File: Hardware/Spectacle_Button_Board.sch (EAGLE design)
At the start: 53 parts, among them J17 AUDIO-JACK3, J19 FTDI_DEVICE, J20 AUDIO-JACK3, U1 CY8C4146LQI-S422, U2 3.3V/150mA

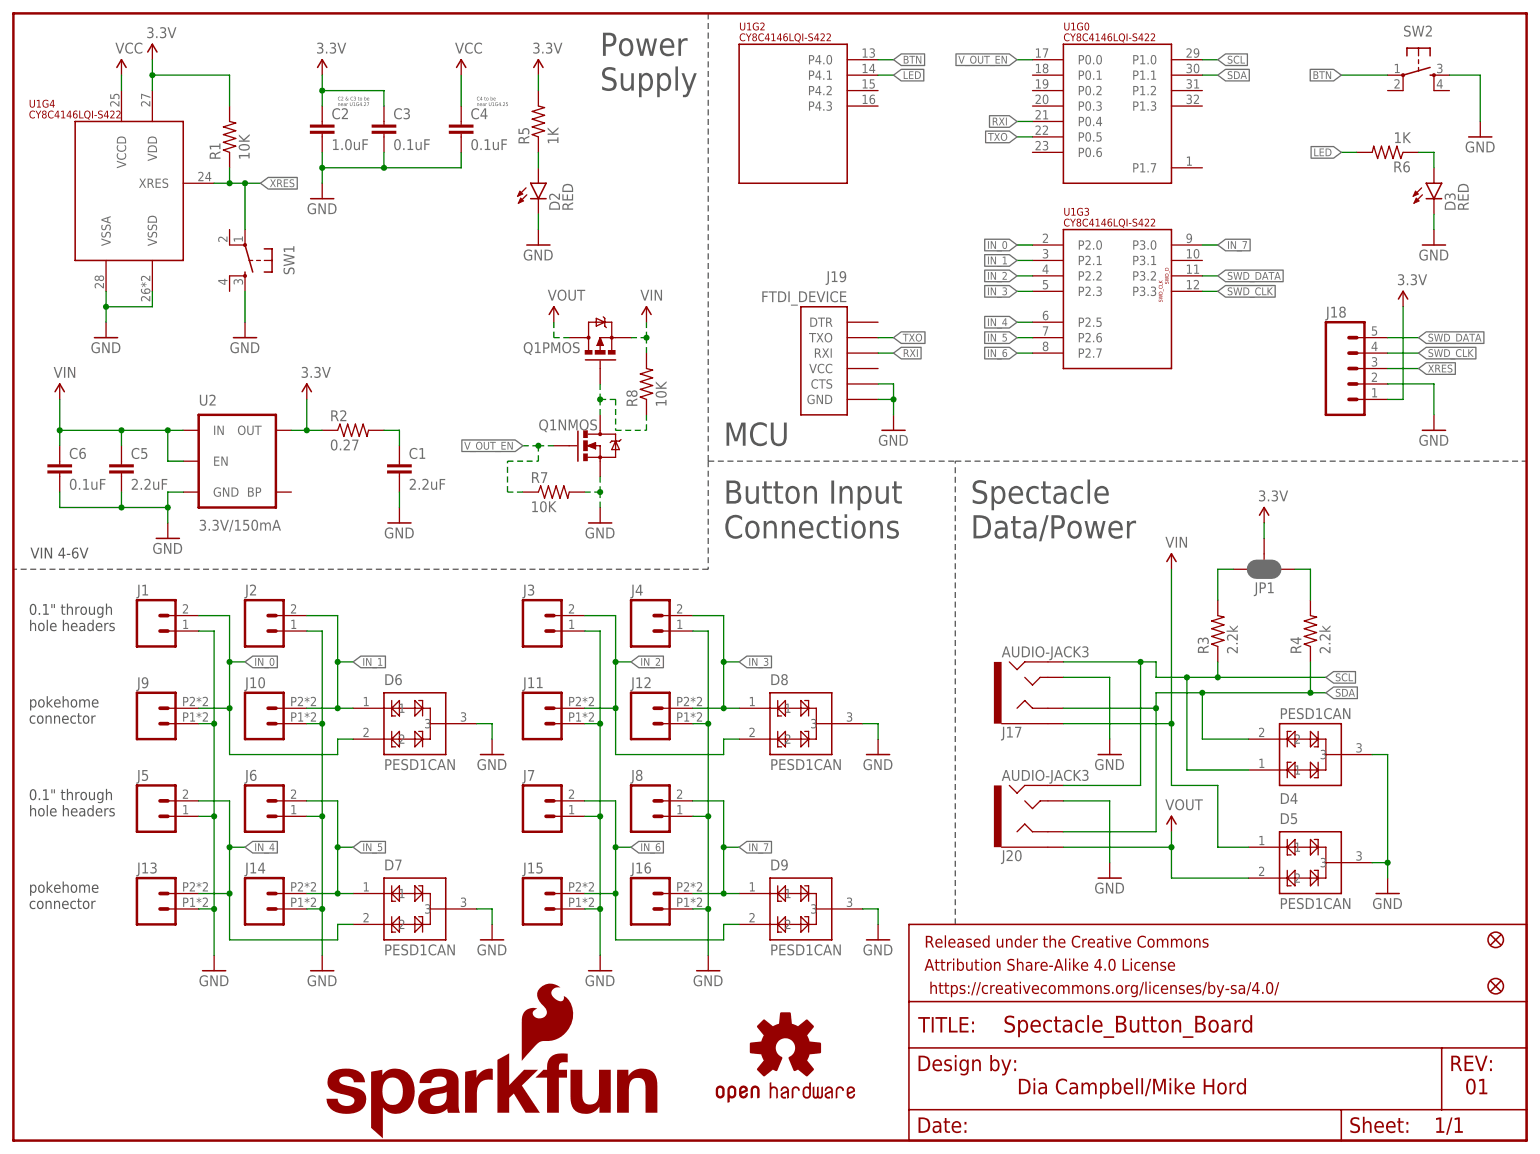
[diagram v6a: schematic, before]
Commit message: Added I2C Mux hardware
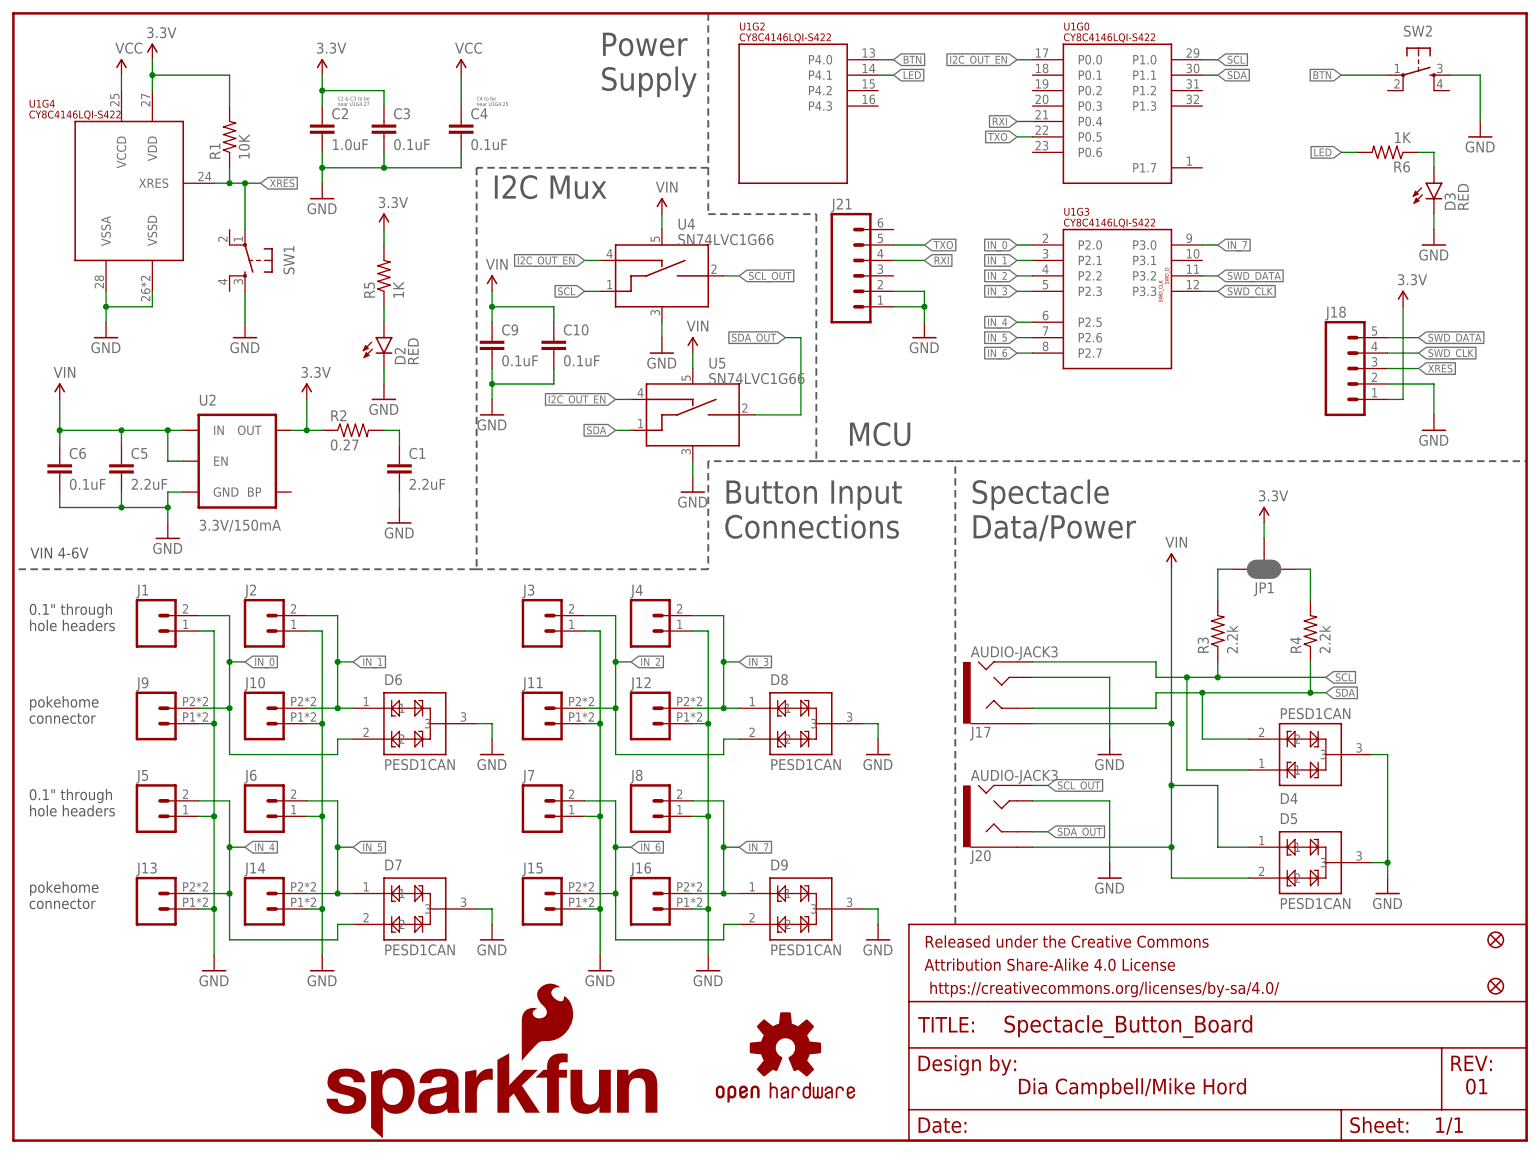
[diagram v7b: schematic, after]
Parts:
- removed J19: FTDI_DEVICE, SparkFun-Connectors:FTDI_DEVICE
- removed Q1: (no value), SparkFun-DiscreteSemi:IRF7509
- removed R7, R8: 10K, SparkFun-Resistors:10KOHM-1/10W-1%(0603)0603
- added C10, C9: 0.1uF, SparkFun-Capacitors:0.1UF-16V(+-10%)(0402)
- added J21: (no value), SparkFun-Connectors:M06NO_SILK_FEMALE_PTH
- added U4, U5: SN74LVC1G66, SparkFun-AnalogIC:SN74LVC1G66_SPST_AMUX
- J18: device SparkFun-Connectors:M05PTH -> SparkFun-Connectors:M05NO_SILK
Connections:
- removed net N$26: Q1NMOS.D, Q1PMOS.G, R8.1
- removed net VOUT: D5.2, J20.EARTH, Q1PMOS.D
- removed net V_OUT_EN: Q1NMOS.G, R7.1, U1G0.P0.0
- new net I2C_OUT_EN: U1G0.P0.0, U4.CTRL_IN, U5.CTRL_IN
- new net SCL_OUT: J20.RING2, U4.A_OUT
- new net SDA_OUT: J20.RING1, U5.A_OUT
- net GND: now also C10.2, C9.2, J21.1, J21.2, U4.VSS, U5.VSS; no longer J19.CTS, J19.GND, Q1NMOS.S, R7.2
- net RXI: now also J21.4; no longer J19.RXI
- net SCL: now also U4.A_IN; no longer J20.RING2
- net SDA: now also U5.A_IN; no longer J20.RING1
- net TXO: now also J21.5; no longer J19.TXO
- net VIN: now also C10.1, C9.1, D5.2, J20.EARTH, U4.VCC, U5.VCC; no longer Q1PMOS.S, R8.2
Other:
- note added: "I2C Mux"
- moved on the sheet: D2, J17, J20, R5

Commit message: Added I2C switching circuitry
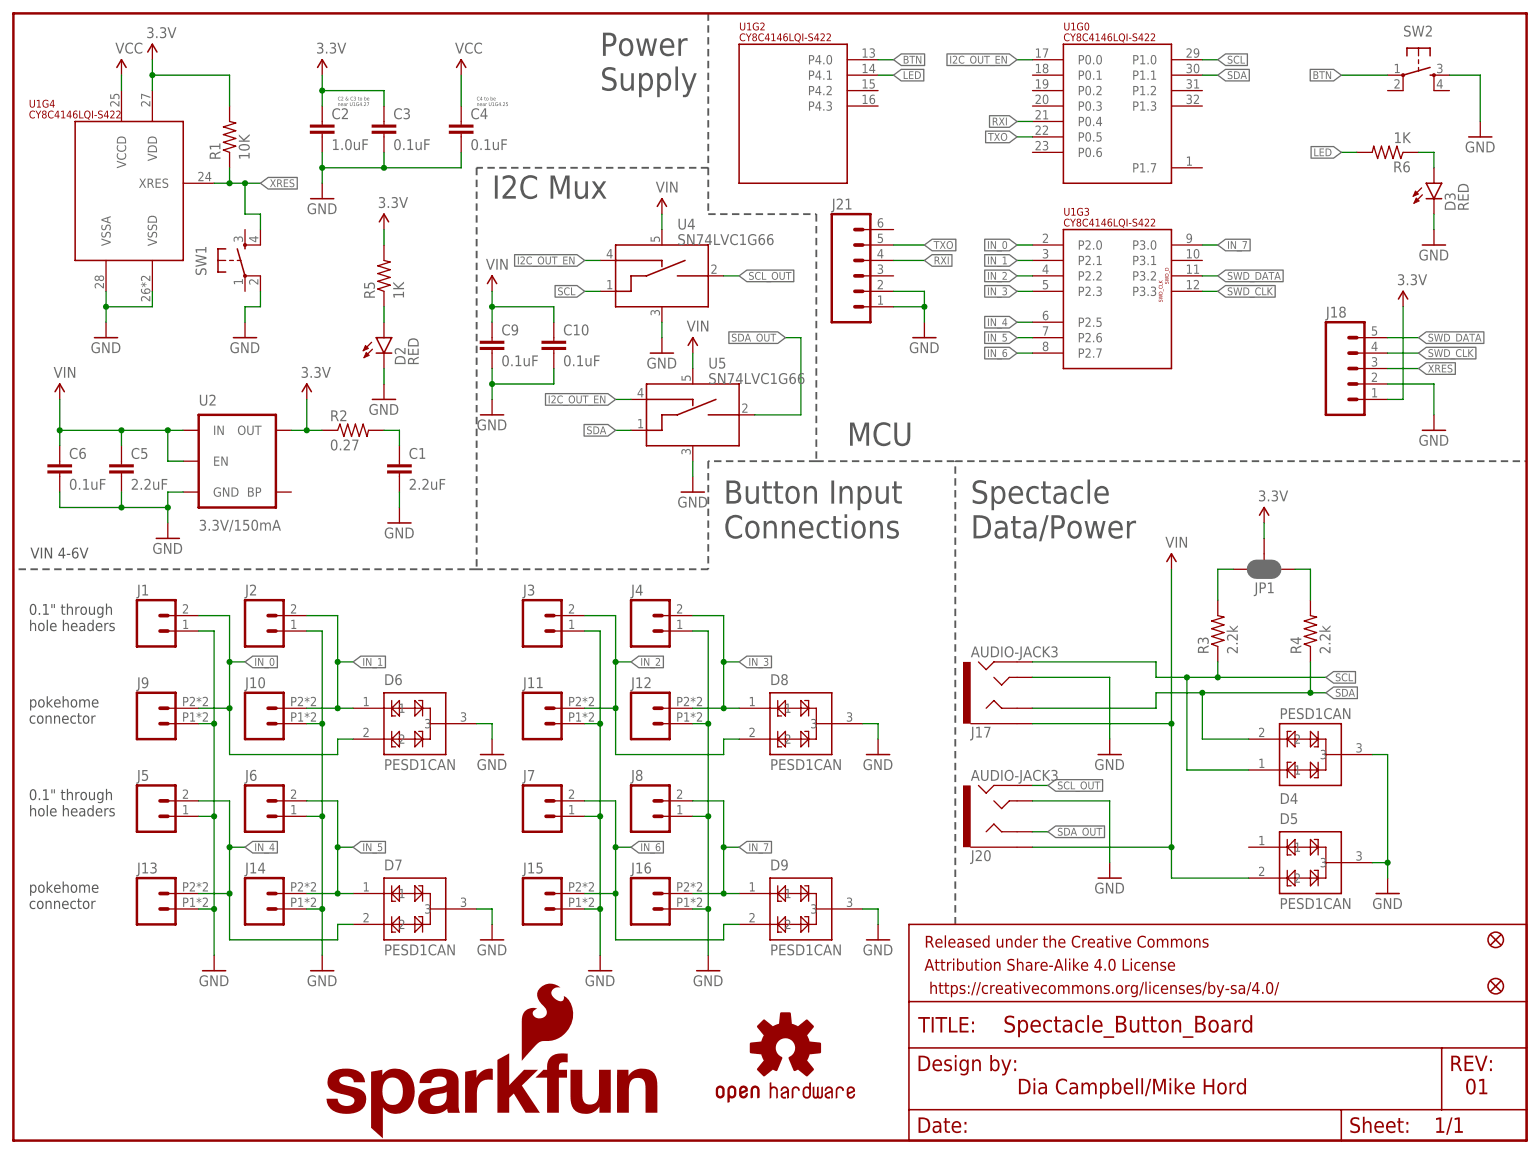
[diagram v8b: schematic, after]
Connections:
- net GND: now also SW1.2; no longer SW1.3
- net VIN: no longer D5.1
- net XRES: now also SW1.4; no longer SW1.1
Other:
- moved on the sheet: SW1
